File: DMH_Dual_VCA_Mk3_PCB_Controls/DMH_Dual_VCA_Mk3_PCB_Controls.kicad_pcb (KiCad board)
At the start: 2 copper layers, 49 x 121 mm, 38 parts, among them J14 Conn_01x06, J15 Conn_01x08, J16 Conn_01x06, J24 Conn_01x08, SW1 SW_DPDT_3way, SW2 SW_DPDT_OnOffOn_x2, U9 TL074

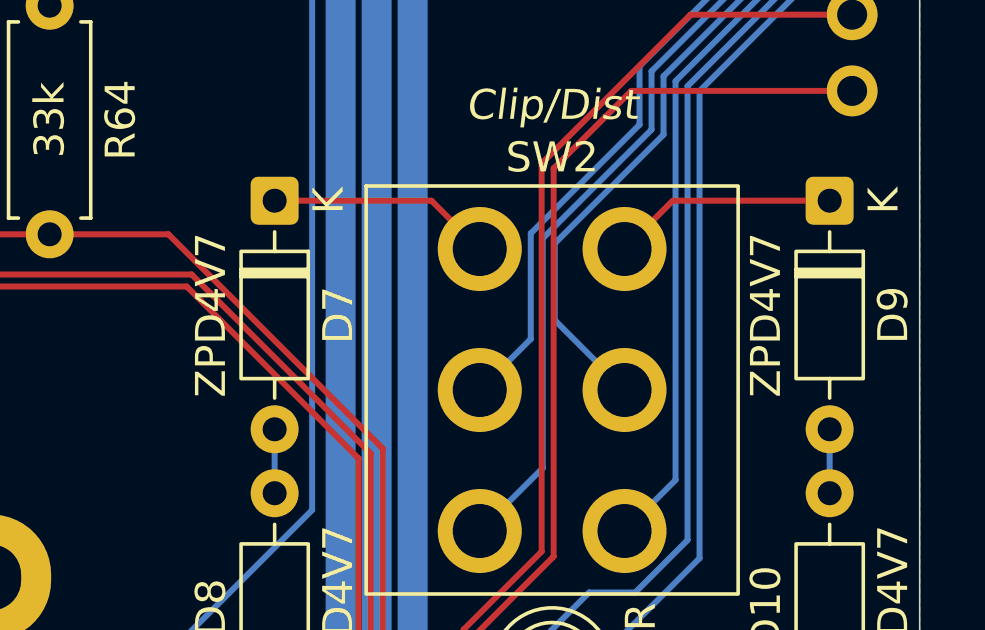
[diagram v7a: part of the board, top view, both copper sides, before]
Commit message: Added jumpers to normalize CV inputs B to A
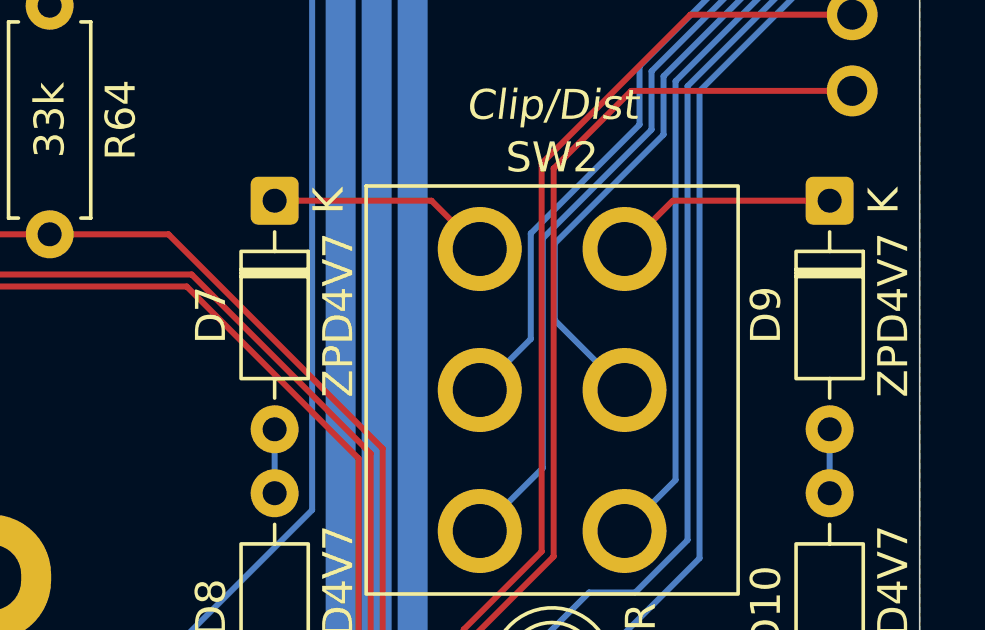
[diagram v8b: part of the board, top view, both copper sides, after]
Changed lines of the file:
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@@
 		(tags "Diode DO-35_SOD27 series Axial Horizontal pin pitch 7.62mm  length 4mm diameter 2mm")
 		(property "Reference" "D9"
+			(at 3.81 2.12 90)
+			(layer "F.SilkS")
+			(effects
+				(font
+					(size 1 1)
+					(thickness 0.15)
+				)
+			)
+		)
+		(property "Value" "ZPD4V7"
 			(at 3.81 -2.12 90)
-			(layer "F.SilkS")
-			(effects
-				(font
-					(size 1 1)
-					(thickness 0.15)
-				)
-			)
-		)
-		(property "Value" "ZPD4V7"
-			(at 3.81 2.12 90)
 			(layer "F.SilkS")
 			(effects
@@
 		(tags "Diode DO-35_SOD27 series Axial Horizontal pin pitch 7.62mm  length 4mm diameter 2mm")
 		(property "Reference" "D7"
+			(at 3.81 2.12 90)
+			(layer "F.SilkS")
+			(effects
+				(font
+					(size 1 1)
+					(thickness 0.15)
+				)
+			)
+		)
+		(property "Value" "ZPD4V7"
 			(at 3.81 -2.12 90)
 			(layer "F.SilkS")
 			(effects
-				(font
-					(size 1 1)
-					(thickness 0.15)
-				)
-			)
-		)
-		(property "Value" "ZPD4V7"
-			(at 3.81 2.12 90)
-			(layer "F.SilkS")
-			(effects
